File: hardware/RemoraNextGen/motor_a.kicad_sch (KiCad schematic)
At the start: 33 parts, among them J3 Motor A phase U, J4 Motor A phase V, J5 Motor A phase W, Q2 CSD16327Q3, Q3 CSD16327Q3, Q4 CSD16327Q3, Q5 CSD16327Q3, Q6 CSD16327Q3, Q7 CSD16327Q3, U4 DRV8300D (A), U5 INA180A2

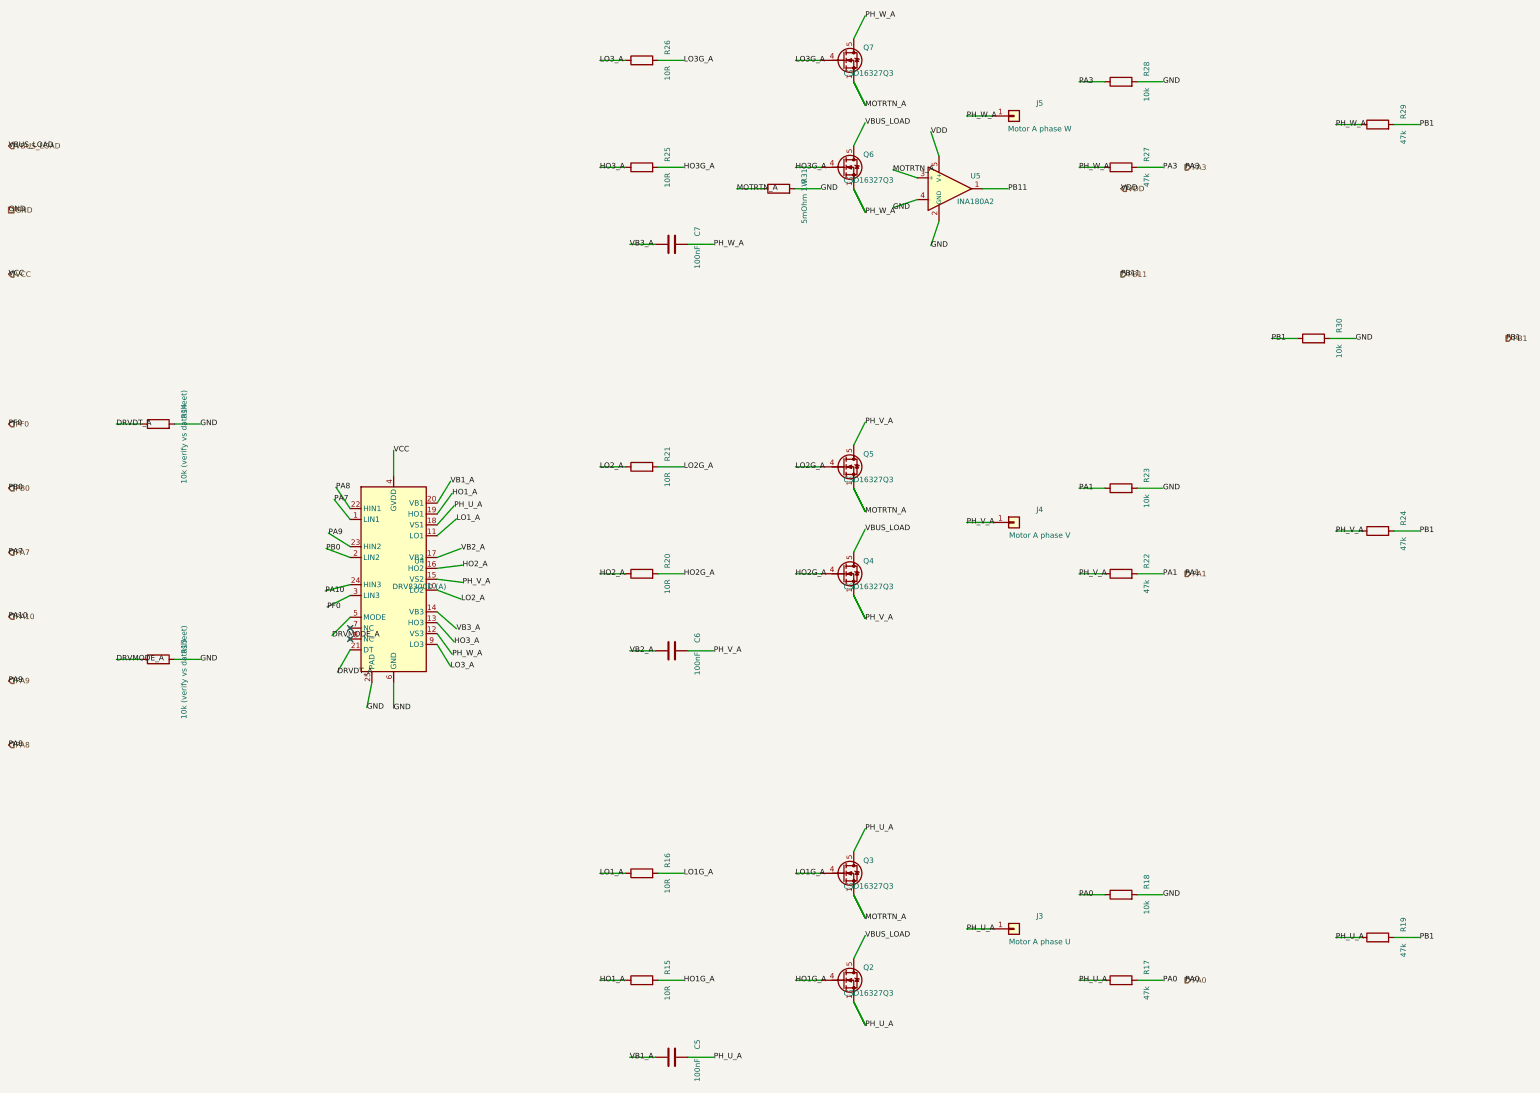
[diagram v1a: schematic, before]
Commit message: Draw real wires instead of floating labels; fix Nucleo lane overlap
Two readability problems, found by actually rendering the generated
schematics to SVG and inspecting them:

- On the root sheet, the 26 Nucleo GPIO/power signals were routed as
  parallel lanes only 4mm apart, each running the full page height.
  ERC was clean, but at any normal zoom they visually merged into an
  unreadable cable bundle. Lanes are now grouped one bundle per
  destination sheet (Power/Motor A/Motor B), with wider in-group
  spacing and a visible gap between groups, sized programmatically
  instead of hardcoded.

- On the power/motor sheets, nearly every net - even between two
  physically adjacent components - was drawn as two disconnected
  stub-wire-and-label islands relying purely on same-name matching,
  never an actual wire. net() now defers to a finalize_nets() pass:
  a net touched at exactly two points gets a real drawn wire (jogged
  if needed); a net touched at 3+ points (GND, VCC, VDD and other
  genuinely pervasive rails) keeps the label convention, matching how
  a real schematic handles shared rails.

Caught a real bug in the first pass at the second fix: a naive
2-segment jog's corner landed exactly on an unrelated VDD hier_label,
silently shorting a motor's current-sense output onto the shared VDD
rail. Fixed by routing jogs through a grid-snapped midpoint instead of
a corner shared with either endpoint's own row/column.

Also ignores *-backups/ (KiCad's own local backup zips).

Co-Authored-By: Claude Sonnet 5 <noreply@anthropic.com>
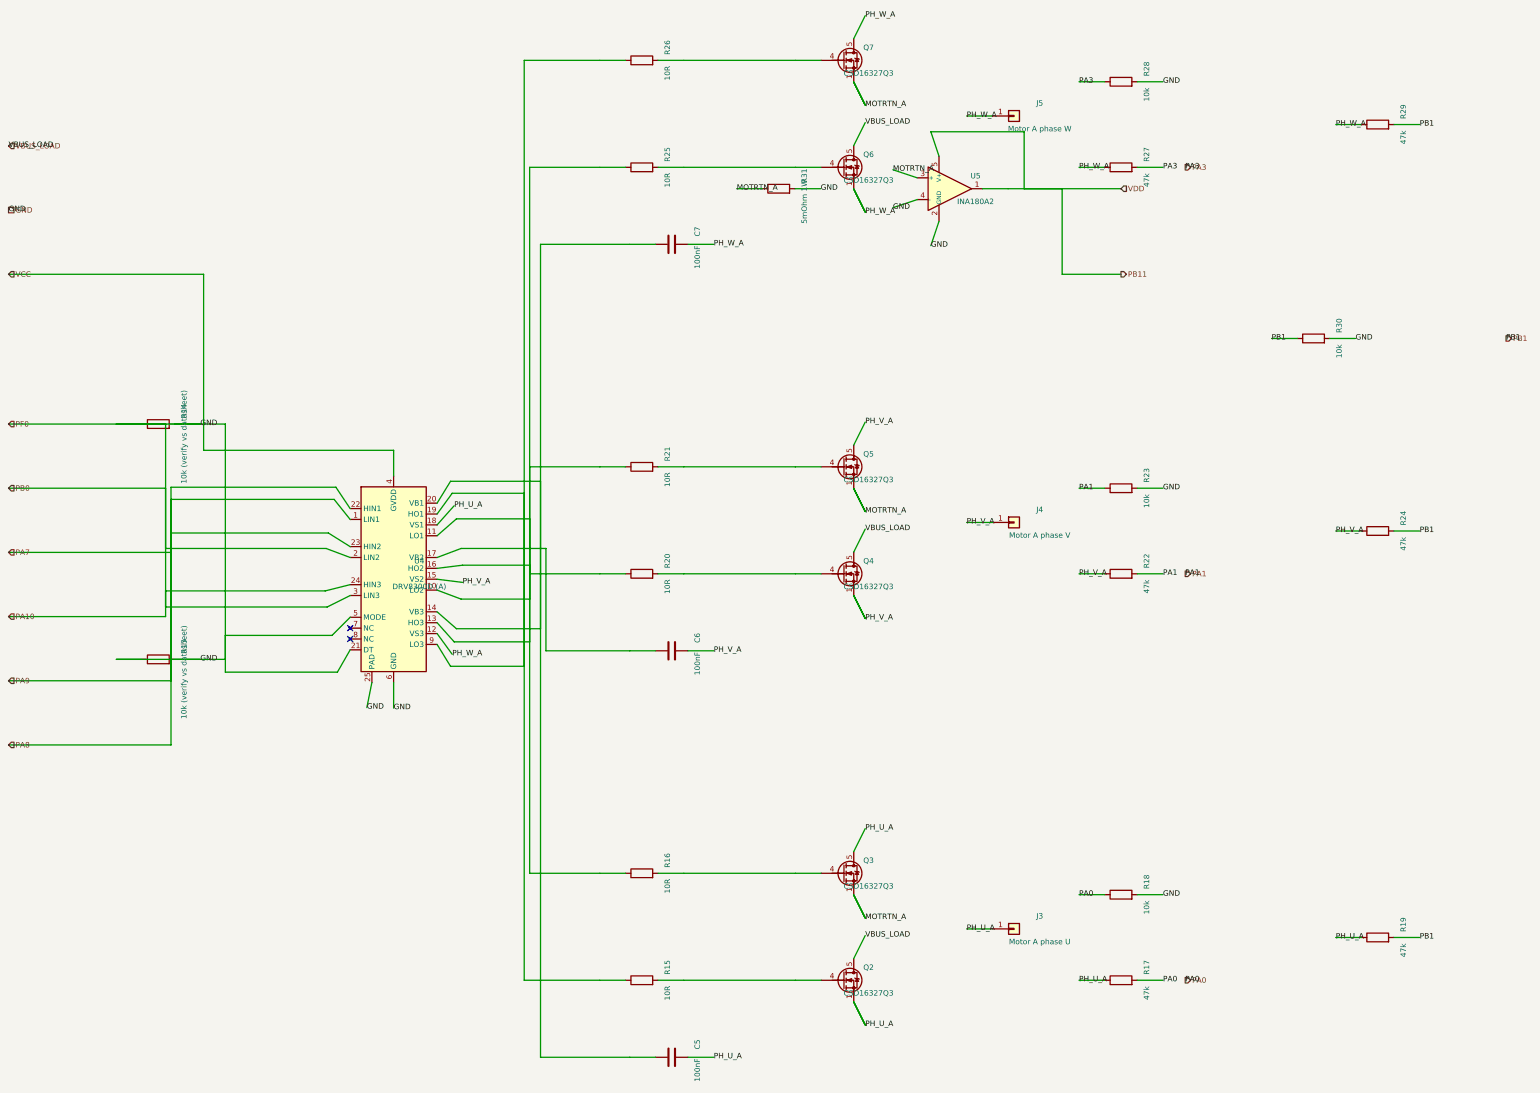
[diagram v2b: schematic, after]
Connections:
- net DRVDT_A is gone; now on net GND: R14.1, U4.21 (DT)
- net DRVMODE_A is gone; now on net GND: R13.1, U4.5 (MODE)
- net HO3_A is gone; now on an unnamed net: R25.1, U4.13 (HO3)
- net LO1_A is gone; now on an unnamed net: R16.1, U4.11 (LO1)
- net LO2_A is gone; now on an unnamed net: R21.1, U4.10 (LO2)
- net LO3_A is gone; now on an unnamed net: R26.1, U4.9 (LO3)
- net PA10 is gone; now on net GND: U4.24 (HIN3)
- net PA8 is gone; now on net PA7: U4.22 (HIN1)
- net PA9 is gone; now on net PA7: U4.23 (HIN2)
- net PB0 is gone; now on net GND: U4.2 (LIN2)
- net PF0 is gone; now on net GND: U4.3 (LIN3)
- net VB3_A is gone; now on an unnamed net: C7.1, U4.14 (VB3)
- net VDD is gone; now on net PB11: U5.5 (V+)
- net HO1G_A: no longer names the net of Q2.4 (G), R15.2
- net HO1_A: no longer names the net of R15.1, U4.19 (HO1)
- net HO2G_A: no longer names the net of Q4.4 (G), R20.2
- net HO2_A: no longer names the net of R20.1, U4.16 (HO2)
- net HO3G_A: no longer names the net of Q6.4 (G), R25.2
- net LO1G_A: no longer names the net of Q3.4 (G), R16.2
- net LO2G_A: no longer names the net of Q5.4 (G), R21.2
- net LO3G_A: no longer names the net of Q7.4 (G), R26.2
- net VB1_A: no longer names the net of C5.1, U4.20 (VB1)
- net VB2_A: no longer names the net of C6.1, U4.17 (VB2)

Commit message: Fit sub-sheet blocks on the page; wire local nets in power schematic
Motor B's sheet box ran from y=610 to y=1010, but the A0 landscape root
page is only 841mm tall - it silently overflowed the bottom edge by
169mm. Motor A/B's box heights (400mm) were also far bigger than their
actual pin content needs (~240mm). Tightened both to 260mm and now
compute each sheet's Y position from the previous one's bottom edge
plus a fixed gap, instead of hardcoded absolute numbers, so this can't
drift out of sync with the page again.

finalize_nets() previously only drew a real wire for nets with exactly
2 points, so every net touched at 3+ points - the majority of the
power schematic - stayed as disconnected floating labels. Now any net
whose points stay within a 150mm span gets chained together with real
wire regardless of point count; only genuinely page-wide rails (GND,
VCC, VDD, VBUS, and similarly wide-spanning nets like a motor's phase
node or return net) still fall back to labels, matching how a real
schematic handles shared rails. Verified motor_a/b's wide nets still
correctly fall back to labels rather than turning into a new rats-nest.

ERC still 0 errors throughout.

Also ignores ~*.lck (KiCad's file-open lock markers).

Co-Authored-By: Claude Sonnet 5 <noreply@anthropic.com>
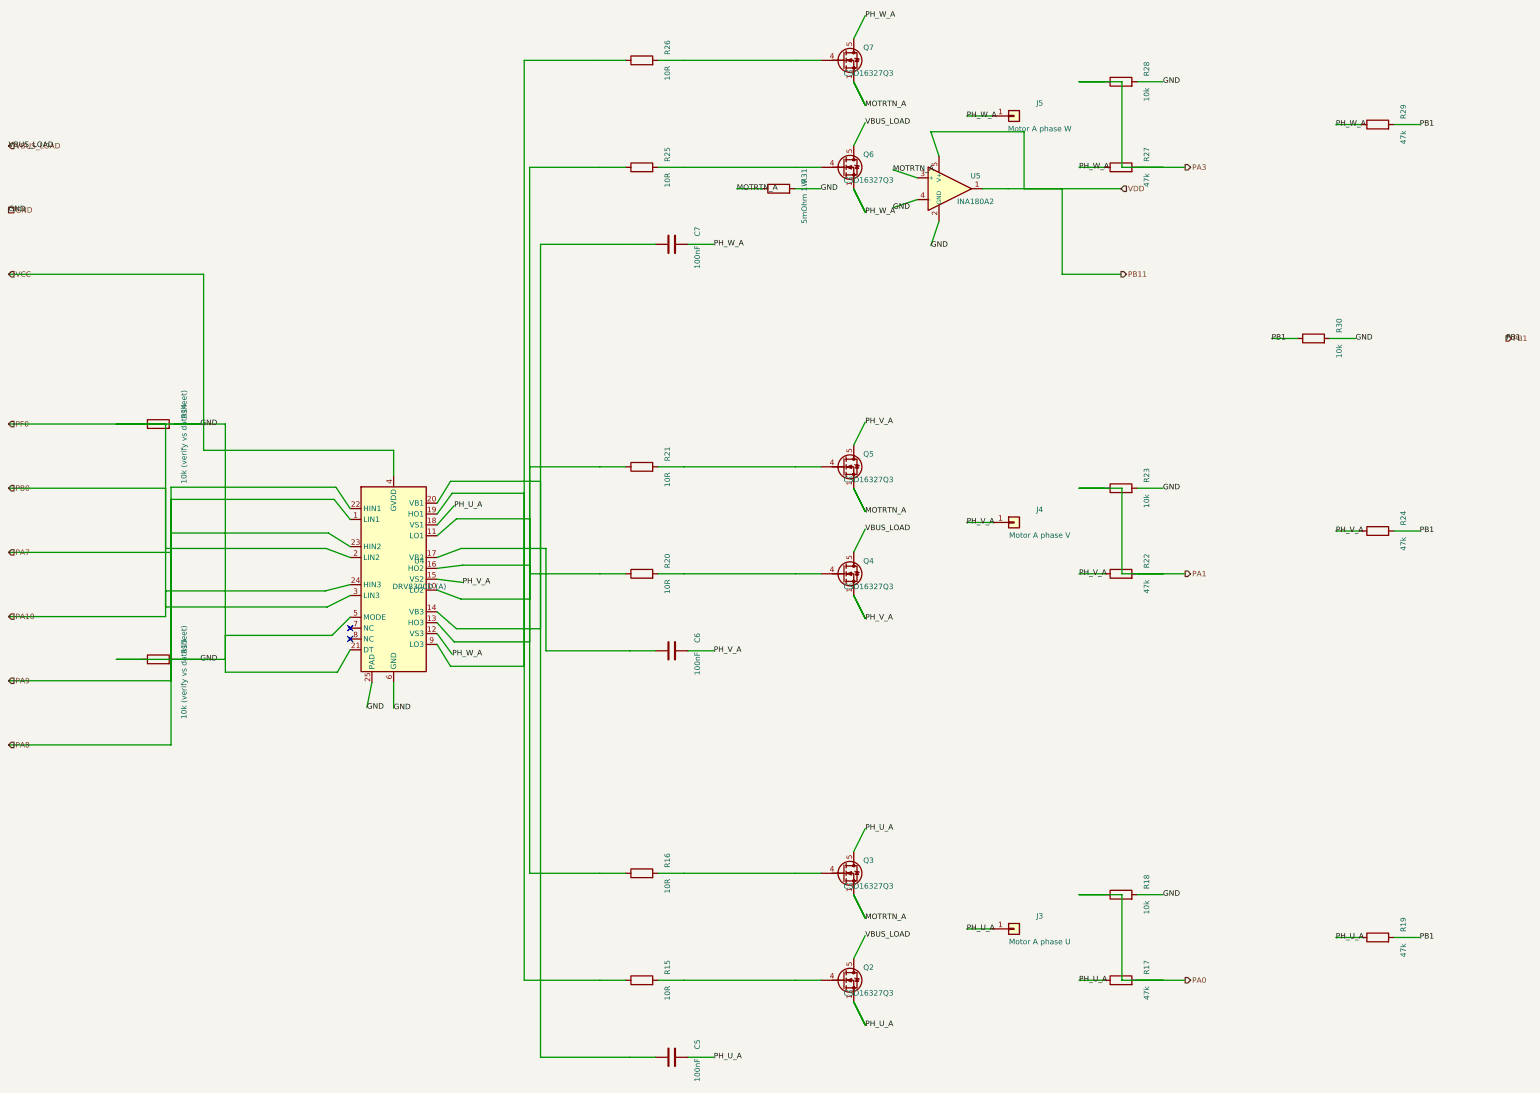
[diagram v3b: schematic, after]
